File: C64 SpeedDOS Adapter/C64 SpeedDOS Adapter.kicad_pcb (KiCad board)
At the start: 2 copper layers, 70.7 x 29 mm, 6 parts, among them J1 C64_User_Port, J2 SpeedDOS, M1 Mounting, M2 Mounting, M3 Mounting, M4 Mounting

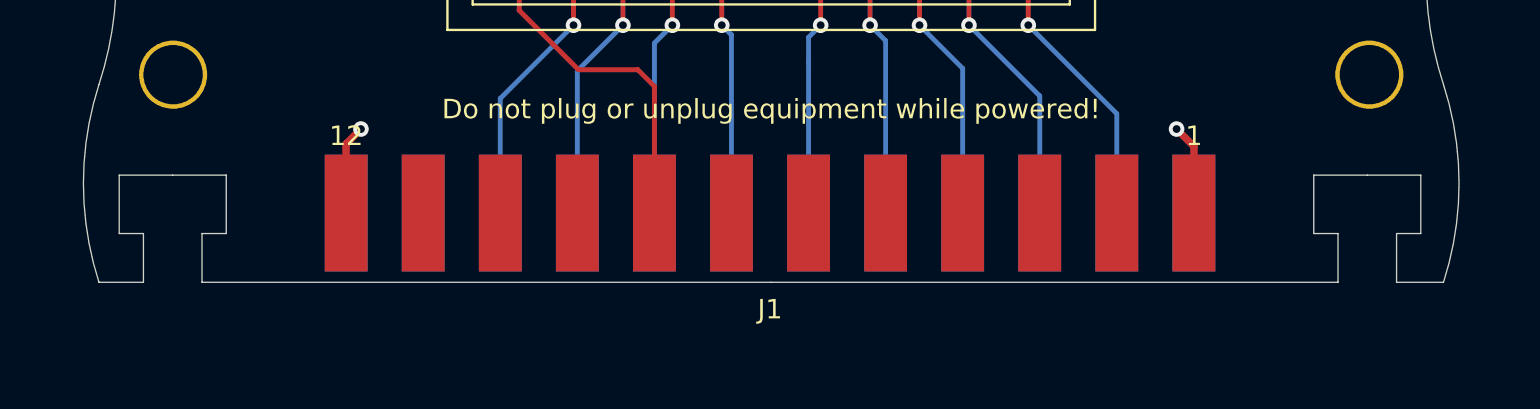
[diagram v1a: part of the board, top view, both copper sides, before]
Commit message: Increase space for M3 nut
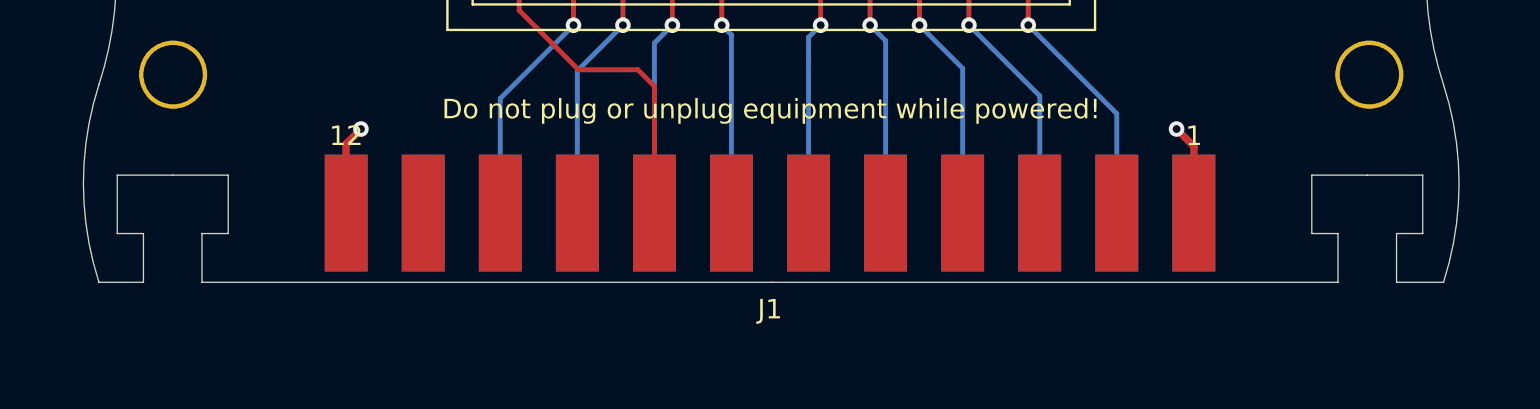
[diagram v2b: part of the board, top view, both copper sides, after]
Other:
- outline, holes or cut-outs redrawn
- board text added: "(read documentation before use)"
- board text added: "Designed for use with C64 1541-II VIA Adapter."
- board text removed: "Designed for use with C64 1541-II VIA Adapter. (read documentation before use)"

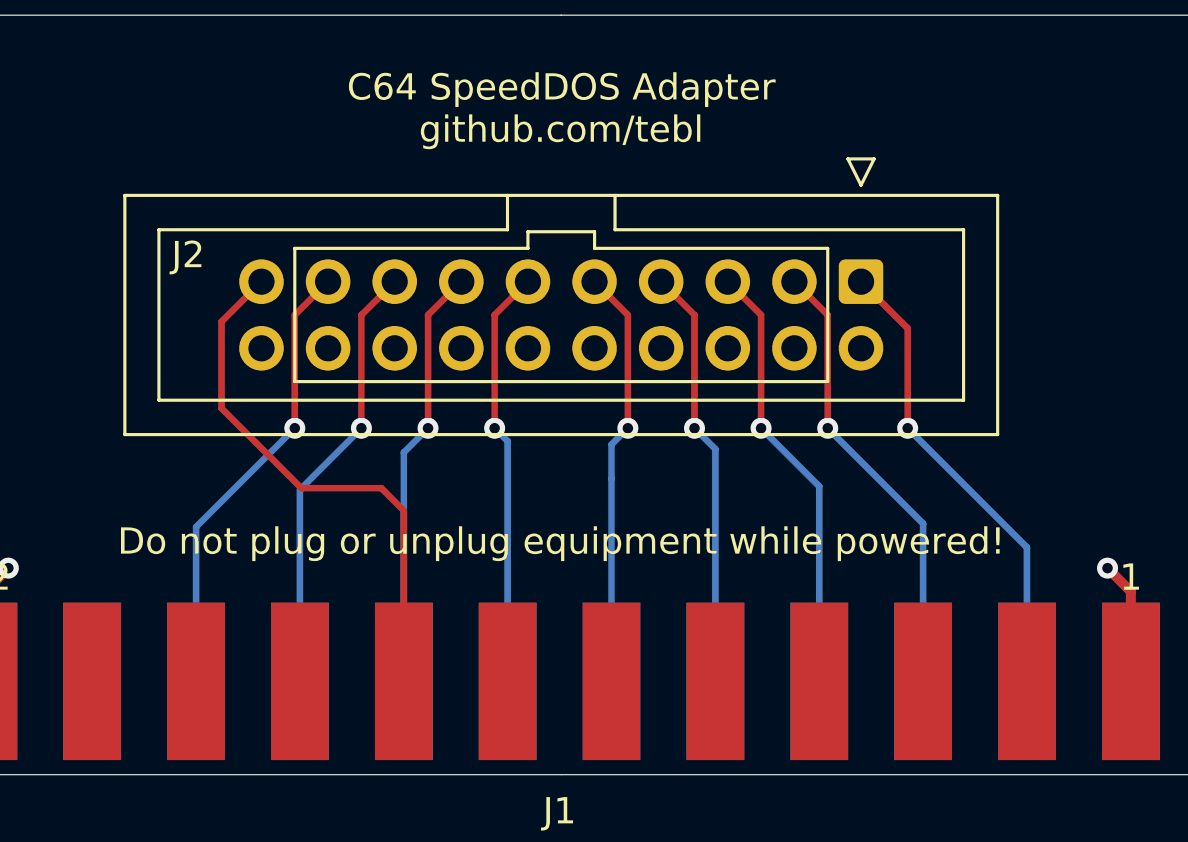
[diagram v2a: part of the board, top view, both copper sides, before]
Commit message: Rotated parallel connector
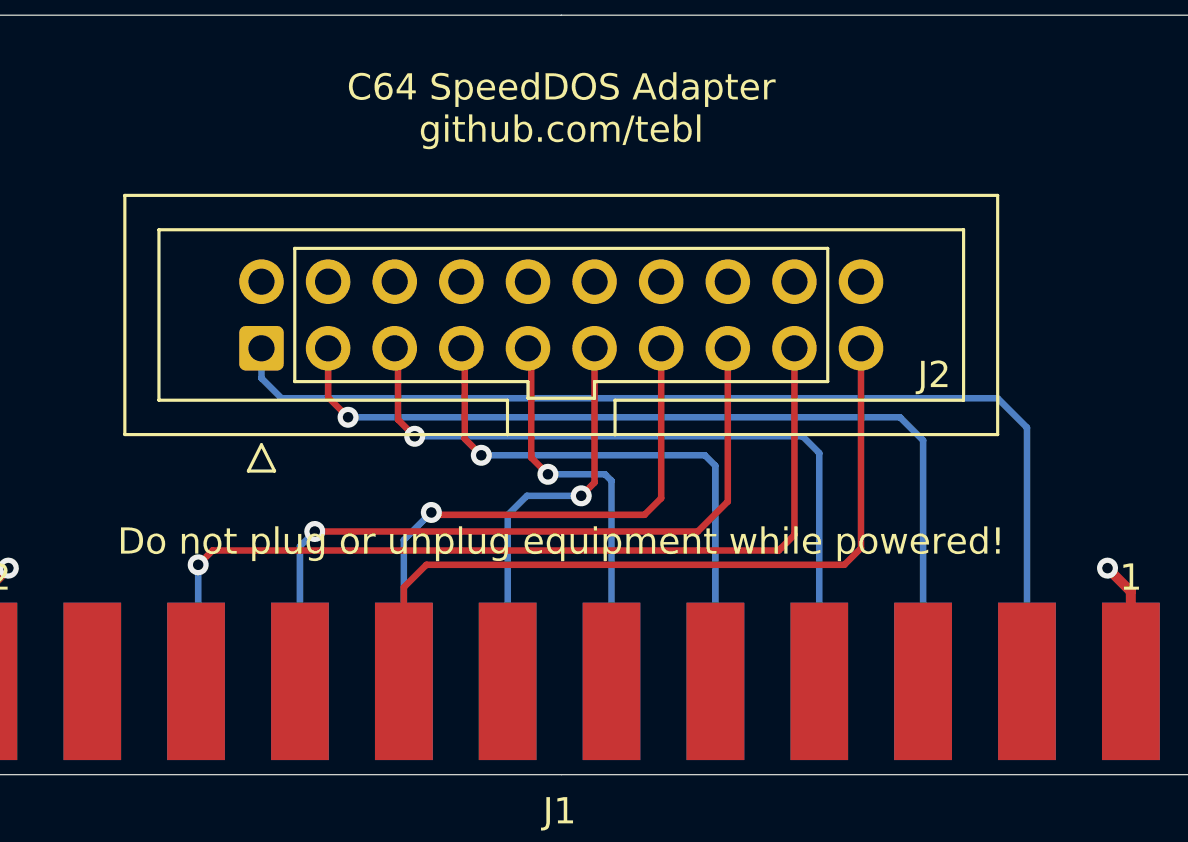
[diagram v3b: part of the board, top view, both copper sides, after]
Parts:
- moved J2 23.0 mm to (140.2, 92.7), turned to 90 degrees
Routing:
- net /VIA_CA2: track 17.9 -> 40.8 mm, vias 1 -> 0
- net /VIA_PA7: track 17.3 -> 34.8 mm
- net /VIA_PA0: track 17.3 -> 34.4 mm
- net /VIA_PA1: track 16.7 -> 28.1 mm
- net /VIA_PA6: track 16.7 -> 28.0 mm
- net /VIA_CB1: track 20.5 -> 29.3 mm
- net /VIA_PA2: track 16.1 -> 21.7 mm
- net /VIA_PA5: track 16.1 -> 21.7 mm
- net /VIA_PA3: track 16.0 -> 15.3 mm
- net /VIA_PA4: track 16.0 -> 15.3 mm

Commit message: Updated gerber files and small tweaks
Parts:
- added JP1: CA2, solder_bridge:bridge, B.Cu at (136.9, 92.2)
- added JP2: CB1, solder_bridge:bridge_r, B.Cu at (166.4, 92.2)
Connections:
- J2 pad 1: /VIA_CA2 -> Net-(J2-Pad1)
- J2 pad 10: /VIA_CB1 -> Net-(J2-Pad10)
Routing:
- net Net-(J2-Pad10): track 0.00 -> 5.05 mm
- net Net-(J2-Pad1): track 0.00 -> 5.05 mm
- net /VIA_CB1: track 29.3 -> 33.1 mm, vias 0 -> 1
- net /VIA_CA2: track 40.8 -> 42.7 mm

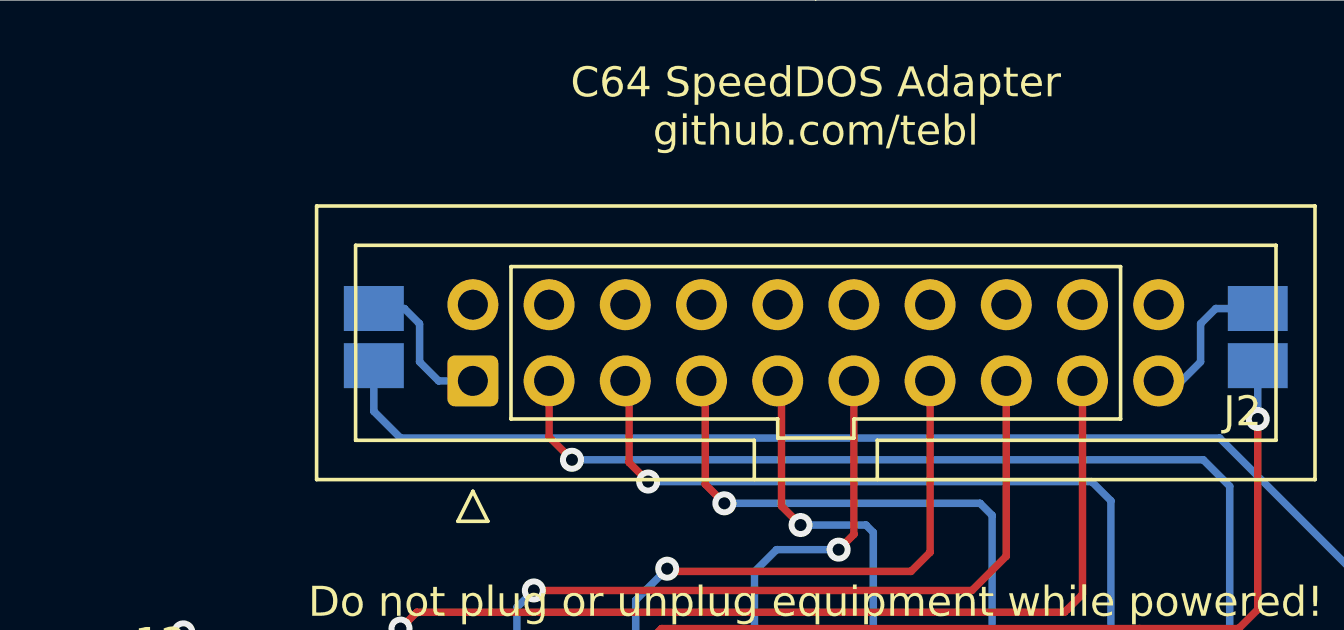
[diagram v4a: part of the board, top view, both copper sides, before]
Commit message: Added GND jumper to adapter
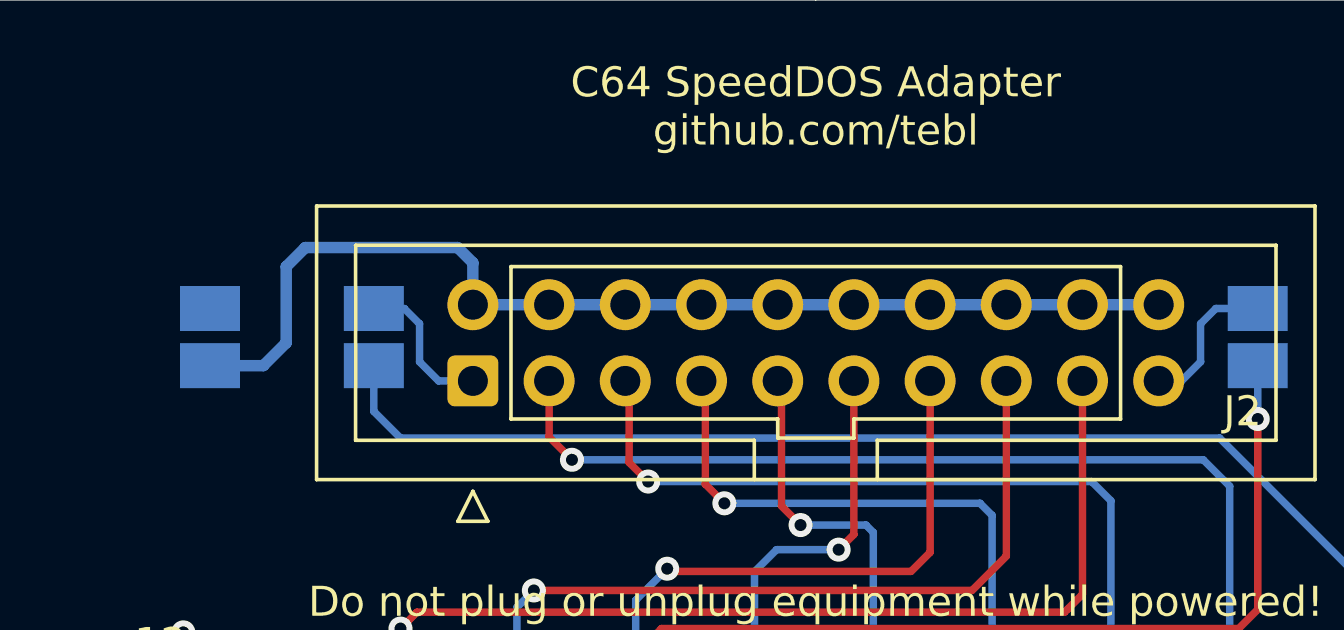
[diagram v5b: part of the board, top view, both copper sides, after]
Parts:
- added JP3: GND, solder_bridge:bridge, B.Cu at (131.4, 92.2)
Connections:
- J2 pad 11: GND -> Net-(J2-Pad11)
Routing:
- net Net-(J2-Pad11): track 0.00 -> 36.3 mm
